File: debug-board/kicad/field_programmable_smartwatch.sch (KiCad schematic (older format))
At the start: 41 parts, among them IC1 BQ24040DSQR, IC2 STM32WB55CEU6, J1 SPI_Header, J2 LPUART_Header, J3 DX07S016JA1R1500, J4 GPIO_Header, Q1 Q_PMOS_DGS, SW2 SW_DIP_x01, Y1 32M, Y2 32.768k

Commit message: Rework debug board design
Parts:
- removed J1: SPI_Header, Connector_PinSocket_2.54mm:PinSocket_1x04_P2.54mm_Vertical, symbol Connector:Conn_01x04_Male
- removed J2: LPUART_Header, Connector_PinHeader_2.54mm:PinHeader_1x02_P2.54mm_Vertical, symbol Connector:Conn_01x02_Male
- removed J4: GPIO_Header, Connector_PinHeader_2.54mm:PinHeader_1x09_P2.54mm_Vertical, symbol Connector:Conn_01x09_Male
- removed SW2: SW_DIP_x01, Button_Switch_SMD:SW_DIP_SPSTx01_Slide_6.7x4.1mm_W6.73mm_P2.54mm_LowProfile_JPin, symbol Switch:SW_DIP_x01
- added J1: GPIO Header 1, Connector_PinHeader_2.54mm:PinHeader_1x12_P2.54mm_Vertical, symbol Connector:Conn_01x12_Male
- added J3: GPIO Header 2, Connector_PinHeader_2.54mm:PinHeader_1x12_P2.54mm_Vertical, symbol Connector:Conn_01x12_Male
- added J4: SWD Header, Connector_PinHeader_2.54mm:PinHeader_1x03_P2.54mm_Vertical, symbol Connector:Conn_01x03_Male
- added R4: 100k, Resistor_SMD:R_0402_1005Metric, symbol Device:R_Small
- added SW1, SW2: SW_Push, Button_Switch_SMD:SW_Push_SPST_NO_Alps_SKRK, symbol Switch:SW_Push
- AE1: footprint TestPoint:TestPoint_Pad_1.0x1.0mm -> W3006:W3006; Item Number (none) -> 1; Manufacturer (none) -> PulseLarsen Antennas; Mfg Part # (none) -> W3006; Package (none) -> 2-SMD, No Lead; Type (none) -> SMD
- BT1: Item Number (none) -> 2
- C1: Manufacturer (none) -> Murata Electronics; Mfg Part # (none) -> GCG188L8EE105KA07D; Package (none) -> 0603; Type (none) -> SMD
- C10: renamed from C5; Manufacturer (none) -> Murata Electronics; Mfg Part # (none) -> GCG188L8EE105KA07D; Package (none) -> 0603; Type (none) -> SMD
- C11: renamed from C9; Manufacturer (none) -> Murata Electronics; Mfg Part # (none) -> GCM155R71C104KA55D; Package (none) -> 0402; Type (none) -> SMD
- C12: renamed from C20; Manufacturer (none) -> Murata Electronics; Mfg Part # (none) -> GCG188L8EE105KA07D; Package (none) -> 0603; Type (none) -> SMD
- C13: renamed from C10; Manufacturer (none) -> Murata Electronics; Mfg Part # (none) -> GCM155R71C104KA55D; Package (none) -> 0402; Type (none) -> SMD
- C14: renamed from C11; Manufacturer (none) -> Murata Electronics; Mfg Part # (none) -> GRM035R60J475ME15J; Package (none) -> 0402; Type (none) -> SMD
- C15: renamed from C21; Manufacturer (none) -> Murata Electronics; Mfg Part # (none) -> GRM155C81E105ME11J; Package (none) -> 0402; Type (none) -> SMD
- C16: Manufacturer (none) -> Murata Electronics; Mfg Part # (none) -> GCQ1555C1H110GB01D; Package (none) -> 0402; Type (none) -> SMD
- C17: renamed from C18; Manufacturer (none) -> Murata Electronics; Mfg Part # (none) -> GCQ1555C1H110GB01D; Package (none) -> 0402; Type (none) -> SMD
- C2: renamed from C6; Manufacturer (none) -> Murata Electronics; Mfg Part # (none) -> GCM155R71C104KA55D; Package (none) -> 0402; Type (none) -> SMD
- C3: renamed from C13; Manufacturer (none) -> KEMET; Mfg Part # (none) -> C0402C101J5GAC7411; Package (none) -> 0402; Type (none) -> SMD
- C4: renamed from C17; Manufacturer (none) -> Murata Electronics; Mfg Part # (none) -> GCM155R71C104KA55D; Package (none) -> 0402; Type (none) -> SMD
- C5: renamed from C7; Manufacturer (none) -> Murata Electronics; Mfg Part # (none) -> GCM155R71C104KA55D; Package (none) -> 0402; Type (none) -> SMD
- C6: renamed from C14; Manufacturer (none) -> Murata Electronics; Mfg Part # (none) -> GCM155R71C104KA55D; Package (none) -> 0402; Type (none) -> SMD
- C7: renamed from C19; Manufacturer (none) -> Murata Electronics; Mfg Part # (none) -> GRM035R60J475ME15J; Package (none) -> 0402; Type (none) -> SMD
- C8: Manufacturer (none) -> Murata Electronics; Mfg Part # (none) -> GCM155R71C104KA55D; Package (none) -> 0402; Type (none) -> SMD
- C9: renamed from C12; Manufacturer (none) -> Murata Electronics; Mfg Part # (none) -> GCM155R71C104KA55D; Package (none) -> 0402; Type (none) -> SMD
- D1: value LED_Small -> LED_Small_Red; Manufacturer (none) -> Wurth Elektronik; Mfg Part # (none) -> 155060SS75300; Package (none) -> 0603; Type (none) -> SMD
- D2: value LED_Small -> LED_Small_Green; Manufacturer (none) -> Wurth Elektronik; Mfg Part # (none) -> 155060VS75300; Package (none) -> 0603; Type (none) -> SMD
- FB1: Manufacturer (none) -> Walsin; Mfg Part # (none) -> WLBD1608K1U601TB; Package (none) -> 0603; Type (none) -> SMD
- FL1: Manufacturer (none) -> STMicroelectronics; Mfg Part # (none) -> MLPF-WB55-01E3; Package (none) -> BumplessCSP-6; Type (none) -> SMD
- IC1: symbol BQ24040DSQR:BQ24040DSQR -> field_programmable_smartwatch-rescue:BQ24040DSQR-BQ24040DSQR; Manufacturer (none) -> Texas Instruments; Mfg Part # (none) -> BQ24040DSQR; Package (none) -> WSON-10; Type (none) -> SMD
- IC2: symbol STM32WB55CEU6:STM32WB55CEU6 -> field_programmable_smartwatch-rescue:STM32WB55CEU6-STM32WB55CEU6; Manufacturer (none) -> STMicroelectronics; Mfg Part # (none) -> STM32WB55CEU6; Package (none) -> UFQFPN-48; Type (none) -> SMD
- J2: renamed from J3; symbol DX07S016JA1R1500:DX07S016JA1R1500 -> field_programmable_smartwatch-rescue:DX07S016JA1R1500-DX07S016JA1R1500; Manufacturer (none) -> JAE Electronics; Mfg Part # (none) -> DX07S016JA1R1500; Type (none) -> SMD/Through hole
- L1: Manufacturer (none) -> TDK; Mfg Part # (none) -> MLJ1005HXG91NJTD0B; Package (none) -> 0402; Type (none) -> SMD
- PS1: symbol LD39050PU33R:LD39050PU33R -> field_programmable_smartwatch-rescue:LD39050PU33R-LD39050PU33R; Manufacturer (none) -> STMicroelectronics; Mfg Part # (none) -> LD39050PU33R; Package (none) -> DFN-6; Type (none) -> SMD
- Q1: Manufacturer (none) -> Toshiba; Mfg Part # (none) -> SSM3J325F,LF; Package (none) -> SOT-346-3; Type (none) -> SMD
- R1: renamed from R7; Manufacturer (none) -> Murata Electronics; Mfg Part # (none) -> NCU15WF104D60RC; Package (none) -> 0402; Type (none) -> SMD
- R2: renamed from R9; Manufacturer (none) -> Panasonic; Mfg Part # (none) -> ERJ-2RHD512X; Package (none) -> 0402; Type (none) -> SMD
- R3: renamed from R1; Manufacturer (none) -> Panasonic; Mfg Part # (none) -> ERJ-2RKF2871X; Package (none) -> 0402; Type (none) -> SMD
- R5: renamed from R2; Manufacturer (none) -> Panasonic; Mfg Part # (none) -> ERA-2VEB2201X; Package (none) -> 0402; Type (none) -> SMD
- R6: renamed from R3; Manufacturer (none) -> Panasonic; Mfg Part # (none) -> ERA-2VEB1501X; Package (none) -> 0603; Type (none) -> SMD
- R7: renamed from R6; Manufacturer (none) -> Panasonic; Mfg Part # (none) -> ERA-2VEB1501X; Package (none) -> 0603; Type (none) -> SMD
- Y1: Manufacturer (none) -> NDK America, Inc.; Mfg Part # (none) -> NX2016SA-32MHZ-EXS00A-CS11336; Package (none) -> 4-SMD, No Lead; Type (none) -> SMD
- Y2: Manufacturer (none) -> NDK America, Inc.; Mfg Part # (none) -> NX3215SA-32.768K-STD-MUA-14; Package (none) -> 2-SMD, No Lead; Type (none) -> SMD
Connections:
- net labels added: OSC32M_IN, OSC32M_OUT, OSC32k_IN, OSC32k_OUT, PA0, PA1, PA10, PA13, PA2, PA3, PA4, PA5, PA6, PA7, PA8, PA9, PB0, PB1, PB2, PB8, PB9, RESET
- net labels removed: LPUART_RX, LPUART_TX, MISO, MOSI, NSS, OSC32_IN, OSC32_OUT, OSC_IN, OSC_OUT, SCK
- wire segments 142 -> 166
- no-connect marks 25 -> 13
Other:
- moved on the sheet: R1

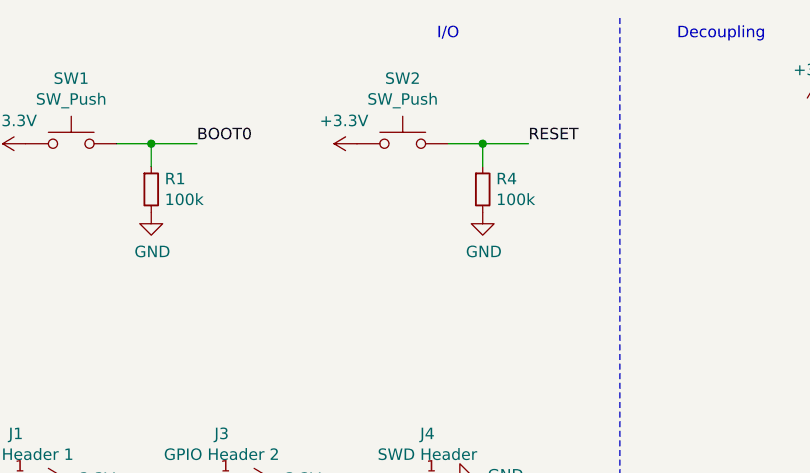
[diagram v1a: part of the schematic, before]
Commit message: Set via on reset button to GND instead of 3.3V
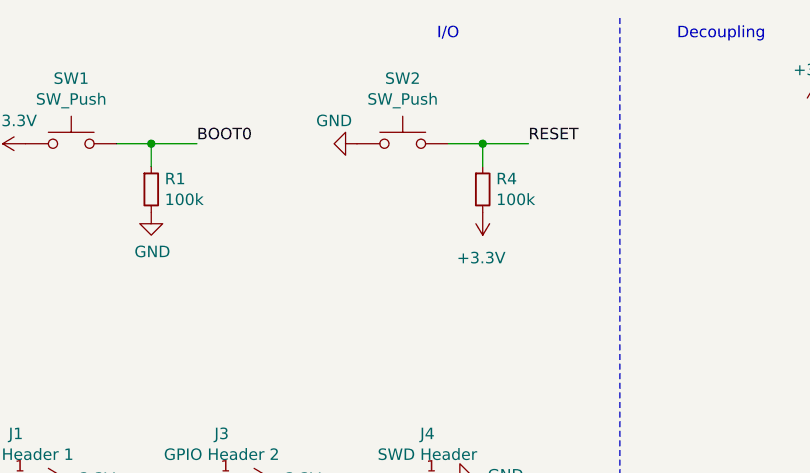
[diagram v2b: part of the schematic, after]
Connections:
- net +3V3: now also R4.2; no longer SW2.1
- net GND: now also SW2.1; no longer R4.2
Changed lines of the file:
@@
 L power:GND #PWR013
 U 1 1 6071B84D
-P 2800 1350
-F 0 "#PWR013" H 2800 1100 50  0001 C CNN
-F 1 "GND" H 2805 1177 50  0000 C CNN
-F 2 "" H 2800 1350 50  0001 C CNN
-F 3 "" H 2800 1350 50  0001 C CNN
-	1    2800 1350
-	1    0    0    -1
+P 2250 1050
+F 0 "#PWR013" H 2250 800 50  0001 C CNN
+F 1 "GND" V 2150 950 50  0000 C CNN
+F 2 "" H 2250 1050 50  0001 C CNN
+F 3 "" H 2250 1050 50  0001 C CNN
+	1    2250 1050
+	0    1    1    0
 $EndComp
 Wire Wire Line
@@
 Wire Wire Line
 	2800 1050 2800 1150
-$Comp
-L power:+3.3V #PWR010
-U 1 1 6071B859
-P 2250 1050
-F 0 "#PWR010" H 2250 900 50  0001 C CNN
-F 1 "+3.3V" V 2350 1000 50  0000 L CNN
-F 2 "" H 2250 1050 50  0001 C CNN
-F 3 "" H 2250 1050 50  0001 C CNN
-	1    2250 1050
-	0    -1   -1   0
-$EndComp
 $Comp
 L Device:R_Small R4
@@
 Wire Wire Line
 	8250 4400 8450 4400
+$Comp
+L power:+3.3V #PWR010
+U 1 1 6071B859
+P 2800 1350
+F 0 "#PWR010" H 2800 1200 50  0001 C CNN
+F 1 "+3.3V" H 2700 1550 50  0000 L CNN
+F 2 "" H 2800 1350 50  0001 C CNN
+F 3 "" H 2800 1350 50  0001 C CNN
+	1    2800 1350
+	-1   0    0    1
+$EndComp
 $EndSCHEMATC

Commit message: Updated debug board
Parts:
- removed BT1: 3.7, Connector_PinHeader_2.54mm:PinHeader_1x02_P2.54mm_Vertical, symbol Device:Battery_Cell
- removed C1, C10: 1u, Capacitor_SMD:C_0603_1608Metric, symbol Device:C_Small
- removed D1: LED_Small_Red, Diode_SMD:D_0603_1608Metric, symbol Device:LED_Small
- removed D2: LED_Small_Green, Diode_SMD:D_0603_1608Metric, symbol Device:LED_Small
- removed IC1: BQ24040DSQR, BQ2404DSQR:SON40P200X200X80-11N, symbol field_programmable_smartwatch-rescue:BQ24040DSQR-BQ24040DSQR
- removed Q1: Q_PMOS_DGS, SSM3J325F_LF:SSM3J325F_LF, symbol Device:Q_PMOS_DGS
- removed R1: 100k, Resistor_SMD:R_0402_1005Metric, symbol Device:R_Small
- removed R3: 2.87k, Resistor_SMD:R_0402_1005Metric, symbol Device:R_Small
- removed R5: 2k, Resistor_SMD:R_0402_1005Metric, symbol Device:R_Small
- removed R6, R7: 1.5k, Resistor_SMD:R_0603_1608Metric, symbol Device:R_Small
- removed SW1: SW_Push, Button_Switch_SMD:SW_Push_SPST_NO_Alps_SKRK, symbol Switch:SW_Push
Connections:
- no-connect marks 13 -> 12
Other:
- moved on the sheet: C12, C15, PS1

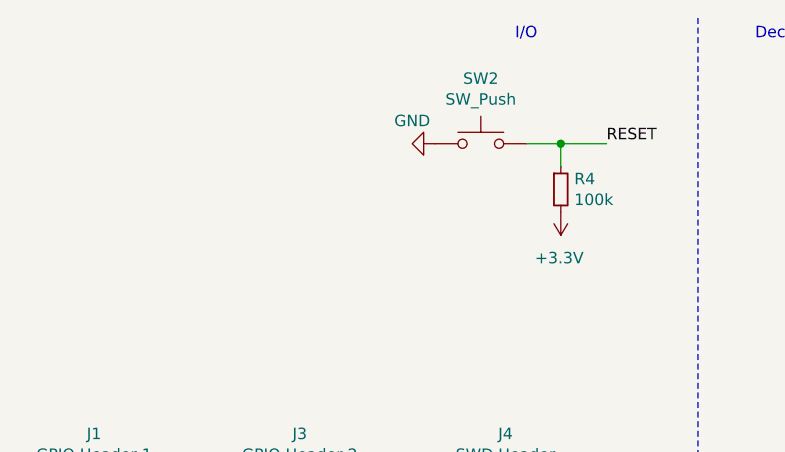
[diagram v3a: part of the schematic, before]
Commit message: Bring back the boot0 pin button
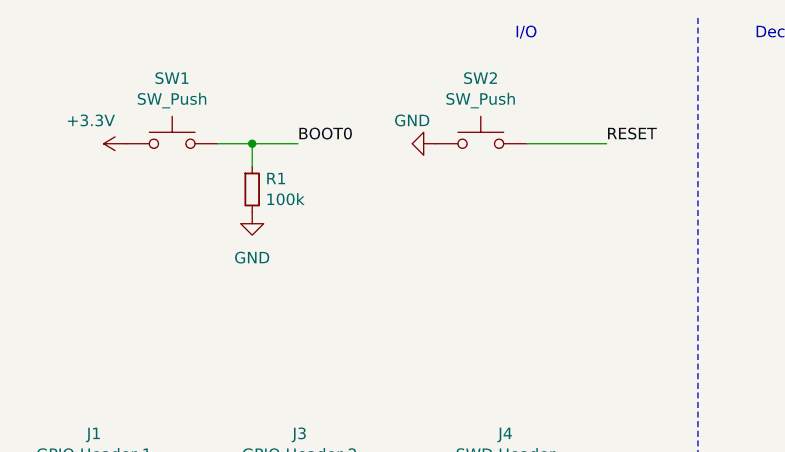
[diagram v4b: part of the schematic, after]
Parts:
- removed R4: 100k, Resistor_SMD:R_0402_1005Metric, symbol Device:R_Small
- added R1: 100k, Resistor_SMD:R_0402_1005Metric, symbol Device:R_Small
- added SW1: SW_Push, Button_Switch_SMD:SW_Push_SPST_NO_Alps_SKRK, symbol Switch:SW_Push
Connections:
- net +3V3: now also SW1.1
- net BOOT0: now also R1.1, SW1.2
- net GND: now also R1.2
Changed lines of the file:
@@
 Text Notes 8250 2800 0    50   ~ 0
 Microcontroller
-Text Notes 2600 600  0    50   ~ 0
-I/O
 Wire Wire Line
 	1200 7550 1300 7550
@@
 Text Label 1900 3600 0    50   ~ 0
 PB9
-Text Label 3000 1050 0    50   ~ 0
-RESET
-Wire Wire Line
-	3000 1050 2800 1050
-Connection ~ 2800 1050
-$Comp
-L power:GND #PWR013
-U 1 1 6071B84D
-P 2250 1050
-F 0 "#PWR013" H 2250 800 50  0001 C CNN
-F 1 "GND" V 2150 950 50  0000 C CNN
-F 2 "" H 2250 1050 50  0001 C CNN
-F 3 "" H 2250 1050 50  0001 C CNN
-	1    2250 1050
-	0    1    1    0
-$EndComp
-Wire Wire Line
-	2800 1050 2650 1050
-Wire Wire Line
-	2800 1050 2800 1150
-$Comp
-L Device:R_Small R4
-U 1 1 6071B865
-P 2800 1250
-F 0 "R4" H 2859 1296 50  0000 L CNN
-F 1 "100k" H 2859 1205 50  0000 L CNN
-F 2 "Resistor_SMD:R_0402_1005Metric" H 2800 1250 50  0001 C CNN
-F 3 "~" H 2800 1250 50  0001 C CNN
-F 4 "C25741" H 2800 1250 50  0001 C CNN "LCSC Part #"
-F 5 "0402WGF1003TCE" H 2800 1250 50  0001 C CNN "Manufacturer_Part_Number"
-F 6 "Murata Electronics" H 2800 1250 50  0001 C CNN "Manufacturer"
-F 7 "NCU15WF104D60RC" H 2800 1250 50  0001 C CNN "Mfg Part #"
-F 8 "0402" H 2800 1250 50  0001 C CNN "Package"
-F 9 "SMD" H 2800 1250 50  0001 C CNN "Type"
-	1    2800 1250
-	1    0    0    -1
-$EndComp
-$Comp
-L Switch:SW_Push SW2
-U 1 1 6071B86F
-P 2450 1050
-F 0 "SW2" H 2450 1335 50  0000 C CNN
-F 1 "SW_Push" H 2450 1244 50  0000 C CNN
-F 2 "Button_Switch_SMD:SW_Push_SPST_NO_Alps_SKRK" H 2450 1250 50  0001 C CNN
-F 3 "~" H 2450 1250 50  0001 C CNN
-F 4 "Alps Alpine" H 2450 1050 50  0001 C CNN "Manufacturer"
-F 5 "SKRKAHE020" H 2450 1050 50  0001 C CNN "Mfg Part #"
-F 6 "SKRK" H 2450 1050 50  0001 C CNN "Package"
-F 7 "SMD" H 2450 1050 50  0001 C CNN "Type"
-	1    2450 1050
-	1    0    0    -1
-$EndComp
 $Comp
 L Connector:Conn_01x12_Male J1
@@
 Wire Wire Line
 	8250 4400 8450 4400
-$Comp
-L power:+3.3V #PWR010
-U 1 1 6071B859
-P 2800 1350
-F 0 "#PWR010" H 2800 1200 50  0001 C CNN
-F 1 "+3.3V" H 2700 1550 50  0000 L CNN
-F 2 "" H 2800 1350 50  0001 C CNN
-F 3 "" H 2800 1350 50  0001 C CNN
-	1    2800 1350
-	-1   0    0    1
-$EndComp
 Connection ~ 1850 6550
 $Comp
@@
 Wire Wire Line
 	1200 5850 3150 5850
+$Comp
+L Switch:SW_Push SW2
+U 1 1 6071B86F
+P 2450 1050
+F 0 "SW2" H 2450 1335 50  0000 C CNN
+F 1 "SW_Push" H 2450 1244 50  0000 C CNN
+F 2 "Button_Switch_SMD:SW_Push_SPST_NO_Alps_SKRK" H 2450 1250 50  0001 C CNN
+F 3 "~" H 2450 1250 50  0001 C CNN
+F 4 "Alps Alpine" H 2450 1050 50  0001 C CNN "Manufacturer"
+F 5 "SKRKAHE020" H 2450 1050 50  0001 C CNN "Mfg Part #"
+F 6 "SKRK" H 2450 1050 50  0001 C CNN "Package"
+F 7 "SMD" H 2450 1050 50  0001 C CNN "Type"
+	1    2450 1050
+	1    0    0    -1
+$EndComp
+$Comp
+L power:GND #PWR013
+U 1 1 6071B84D
+P 2250 1050
+F 0 "#PWR013" H 2250 800 50  0001 C CNN
+F 1 "GND" V 2150 950 50  0000 C CNN
+F 2 "" H 2250 1050 50  0001 C CNN
+F 3 "" H 2250 1050 50  0001 C CNN
+	1    2250 1050
+	0    1    1    0
+$EndComp
+Text Label 3000 1050 0    50   ~ 0
+RESET
+Text Notes 2600 600  0    50   ~ 0
+I/O
+$Comp
+L Device:R_Small R1
+U 1 1 61306B31
+P 1450 1250
+F 0 "R1" H 1509 1296 50  0000 L CNN
+F 1 "100k" H 1509 1205 50  0000 L CNN
+F 2 "Resistor_SMD:R_0402_1005Metric" H 1450 1250 50  0001 C CNN
+F 3 "~" H 1450 1250 50  0001 C CNN
+F 4 "C25741" H 1450 1250 50  0001 C CNN "LCSC Part #"
+F 5 "0402WGF1003TCE" H 1450 1250 50  0001 C CNN "Manufacturer_Part_Number"
+F 6 "Murata Electronics" H 1450 1250 50  0001 C CNN "Manufacturer"
+F 7 "NCU15WF104D60RC" H 1450 1250 50  0001 C CNN "Mfg Part #"
+F 8 "0402" H 1450 1250 50  0001 C CNN "Package"
+F 9 "SMD" H 1450 1250 50  0001 C CNN "Type"
+	1    1450 1250
+	1    0    0    -1
+$EndComp
+$Comp
+L power:+3.3V #PWR01
+U 1 1 61306B37
+P 900 1050
+F 0 "#PWR01" H 900 900 50  0001 C CNN
+F 1 "+3.3V" V 1000 1100 50  0000 L CNN
+F 2 "" H 900 1050 50  0001 C CNN
+F 3 "" H 900 1050 50  0001 C CNN
+	1    900  1050
+	0    -1   -1   0
+$EndComp
+$Comp
+L Switch:SW_Push SW1
+U 1 1 61306B41
+P 1100 1050
+F 0 "SW1" H 1100 1335 50  0000 C CNN
+F 1 "SW_Push" H 1100 1244 50  0000 C CNN
+F 2 "Button_Switch_SMD:SW_Push_SPST_NO_Alps_SKRK" H 1100 1250 50  0001 C CNN
+F 3 "~" H 1100 1250 50  0001 C CNN
+F 4 "Alps Alpine" H 1100 1050 50  0001 C CNN "Manufacturer"
+F 5 "SKRKAHE020" H 1100 1050 50  0001 C CNN "Mfg Part #"
+F 6 "SKRK" H 1100 1050 50  0001 C CNN "Package"
+F 7 "SMD" H 1100 1050 50  0001 C CNN "Type"
+	1    1100 1050
+	1    0    0    -1
+$EndComp
+Wire Wire Line
+	1450 1050 1450 1150
+Wire Wire Line
+	1450 1050 1300 1050
+$Comp
+L power:GND #PWR05
+U 1 1 61306B49
+P 1450 1350
+F 0 "#PWR05" H 1450 1100 50  0001 C CNN
+F 1 "GND" H 1450 1150 50  0000 C CNN
+F 2 "" H 1450 1350 50  0001 C CNN
+F 3 "" H 1450 1350 50  0001 C CNN
+	1    1450 1350
+	1    0    0    -1
+$EndComp
+Connection ~ 1450 1050
+Wire Wire Line
+	1650 1050 1450 1050
+Text Label 1650 1050 0    50   ~ 0
+BOOT0
+Wire Wire Line
+	2650 1050 3000 1050
 $EndSCHEMATC
